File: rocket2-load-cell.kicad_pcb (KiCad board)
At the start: 2 copper layers, 69 x 67 mm, 40 parts, among them J1 SWD, J2 Screw_Terminal_01x02, U2 STM32F103C8Tx, U3 AMS1117-3.3, Y1 16MHz

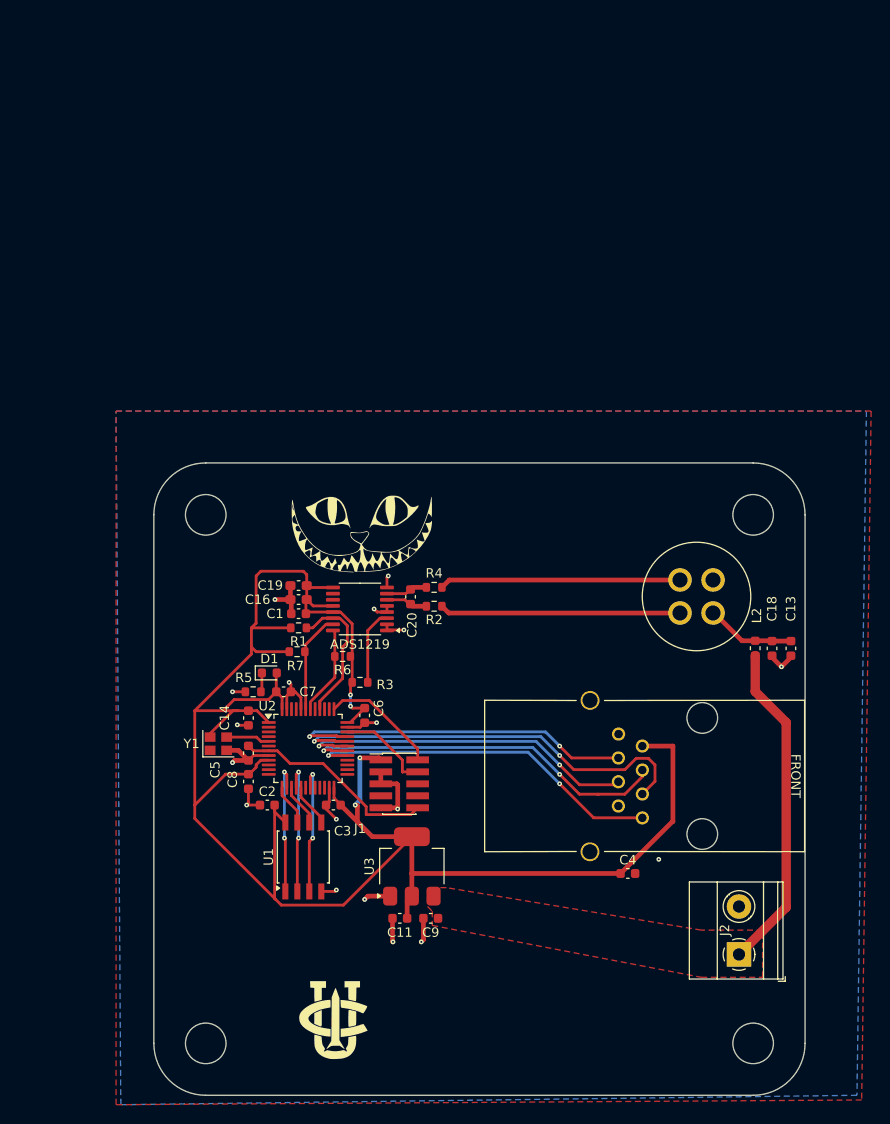
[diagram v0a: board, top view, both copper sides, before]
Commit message: PCB Updates + Schematic Adjustments
Layout, signal lines, and basis for power routing.

Added a voltage divider to the USB_VBUS pin to protect GPIO.
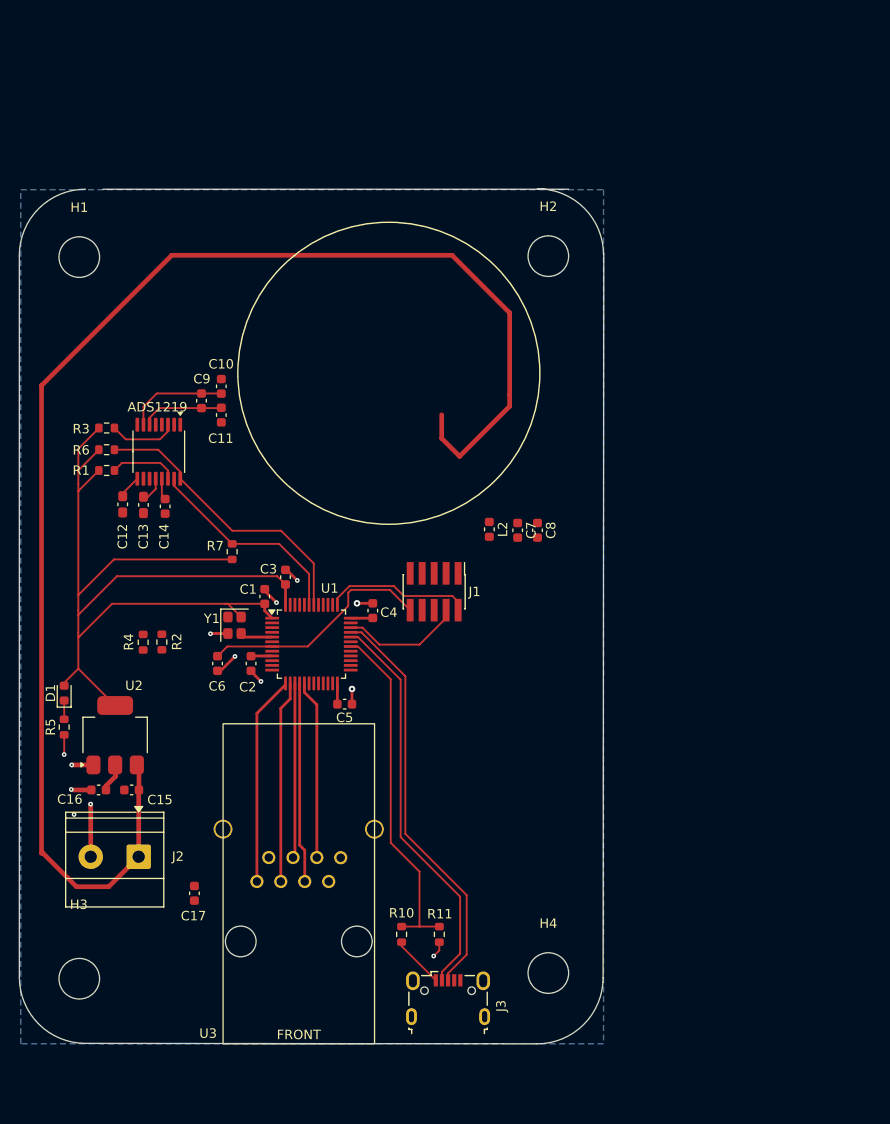
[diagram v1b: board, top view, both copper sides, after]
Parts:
- removed C18: 10uF, Capacitor_SMD:C_0603_1608Metric
- removed C19: 0.1uF, Capacitor_SMD:C_0603_1608Metric_Pad1.08x0.95mm_HandSolder
- removed C20: 0.1uF, Capacitor_SMD:C_0603_1608Metric
- removed G***: LOGO, UCILIB:uci_rocket_logo
- removed G***: LOGO, UCILIB:cat_logo
- removed GX12: ~, UCIRP-KiCAD-Lib:gx12
- removed U5: ~, GSE:GC-XPORT
- added C10: 0.1uF, Capacitor_SMD:C_0603_1608Metric, F.Cu at (127.7, 73.9)
- added C12: 0.1uF, Capacitor_SMD:C_0603_1608Metric_Pad1.08x0.95mm_HandSolder, F.Cu at (117.2, 86.4)
- added C15: 22uF, Capacitor_SMD:C_0603_1608Metric, F.Cu at (118.2, 116.7)
- added C17: 4.7uF, Capacitor_SMD:C_0603_1608Metric, F.Cu at (124.8, 127.6)
- added J3: 629105150521, Connector_USB:USB_Micro-B_Wuerth_629105150521, F.Cu at (151.7, 138.7)
- added R10: 10K, Resistor_SMD:R_0603_1608Metric, F.Cu at (146.8, 131.9)
- added R11: 10K, Resistor_SMD:R_0603_1608Metric, F.Cu at (150.8, 131.9)
- C1: value 0.1uF -> 100nF
- C11, C9: value 22uF -> 0.1uF
- C13: value 100nF -> 0.1uF; footprint Capacitor_SMD:C_0603_1608Metric -> Capacitor_SMD:C_0603_1608Metric_Pad1.08x0.95mm_HandSolder
- C14: value 100nF -> 0.1uF
- C16: value 0.1uF -> 22uF; footprint Capacitor_SMD:C_0603_1608Metric_Pad1.08x0.95mm_HandSolder -> Capacitor_SMD:C_0603_1608Metric
- C4: value 4.7uF -> 100nF
- C8: value 100nF -> 10uF
- R2, R4: value 100 -> 330
- U1: value ~ -> STM32F103C8Tx; footprint Package_SO:SOIC-8W_5.3x5.3mm_P1.27mm -> Package_QFP:LQFP-48_7x7mm_P0.5mm
- U2: value STM32F103C8Tx -> AMS1117-3.3; footprint Package_QFP:LQFP-48_7x7mm_P0.5mm -> Package_TO_SOT_SMD:SOT-223-3_TabPin2
- U3: value AMS1117-3.3 -> ~; footprint Package_TO_SOT_SMD:SOT-223-3_TabPin2 -> UCIRP-KiCAD-Lib:GC-XPORT
- moved H1 109.7 mm to (112.6, 60.2)
- moved H3 86.7 mm to (112.6, 136.7)
- moved C13 70.3 mm to (119.4, 86.5)
- moved J2 64.4 mm to (118.9, 123.7), turned to 180 degrees
- moved C9 60.0 mm to (125.5, 75.4), turned to 90 degrees
- moved C11 56.6 mm to (127.7, 76.9), turned to 90 degrees
- moved H2 45.5 mm to (162.3, 60.1)
- moved C8 40.6 mm to (161.2, 89.1), turned to -90 degrees
- moved C4 38.8 mm to (143.7, 97.7), turned to -90 degrees
- moved R3 38.0 mm to (115.5, 78.3)
- moved H4 37.1 mm to (162.3, 136.1)
- moved R6 33.2 mm to (115.5, 80.6), turned to 0 degrees
- moved R4 31.4 mm to (119.4, 101.0), turned to 90 degrees
- moved L2 30.9 mm to (156.1, 89.0)
- moved C7 30.1 mm to (159.1, 89.1), turned to -90 degrees
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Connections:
- C11 pad 2: +3.3V -> Net-(ADS1219-AIN3)
- C13 pad 1: VLC -> +3.3V
- C16 pad 1: +3.3V -> GND
- C16 pad 2: GND -> +3.3V
- C4 pad 1: +3.3V -> GND
- C4 pad 2: GND -> +3.3V
- C5 pad 2: NRST -> +3.3V
- C6 pad 2: +3.3V -> NRST
- C7 pad 1: GND -> VLC
- C7 pad 2: +3.3V -> GND
- C8 pad 1: GND -> VLC
- C8 pad 2: +3.3V -> GND
- C9 pad 1: GND -> Net-(ADS1219-AIN3)
- C9 pad 2: VBUS -> Net-(ADS1219-AIN2)
- U1 pad 1: MEM_CS -> +3.3V
- U1 pad 2: MEM_MISO -> unconnected-(U1-PC13-Pad2)
- U1 pad 3: MEM_WP -> unconnected-(U1-PC14-Pad3)
- U1 pad 4: GND -> unconnected-(U1-PC15-Pad4)
- U1 pad 5: MEM_MOSI -> HSE_IN
- U1 pad 6: MEM_SCK -> unconnected-(U1-PD1-Pad6)
- U1 pad 7: MEM_HOLD -> NRST
- U1 pad 8: +3.3V -> GND
- U2 pad 1: +3.3V -> GND
- U2 pad 2: unconnected-(U2-PC13-Pad2) -> +3.3V
- U2 pad 3: unconnected-(U2-PC14-Pad3) -> VBUS
- U3 pad 3: VBUS -> ETH_~{RST}
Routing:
- net VBUS: track 35.1 -> 152.9 mm
- net +3.3V: track 214.6 -> 127.8 mm, vias 4 -> 0
- net USB_D+: track 0.00 -> 43.9 mm
- net USB_D-: track 0.00 -> 42.6 mm
- net Net-(U1-PA9): track 0.00 -> 37.1 mm
- net GND: track 55.9 -> 26.5 mm, vias 18 -> 13
- net AIN+: track 25.6 -> 0.00 mm
- net AIN-: track 25.5 -> 0.00 mm
- net ETH_RTS: track 45.8 -> 21.4 mm, vias 2 -> 0
- net ETH_TX: track 40.0 -> 18.5 mm, vias 2 -> 0
- net ADS_CLK: track 9.49 -> 30.9 mm
- net ETH_~{RST}: track 38.2 -> 19.0 mm, vias 2 -> 0
- net ETH_CTS: track 38.3 -> 22.2 mm, vias 2 -> 0
- net ETH_RX: track 36.6 -> 21.2 mm, vias 2 -> 0
- net MEM_MISO: track 14.5 -> 0.00 mm, vias 2 -> 0
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- removed copper zone on F.Cu, net GND
- removed copper zone on F.Cu, net VBUS
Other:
- board size 69 x 67 mm -> 61.9 x 90.6 mm

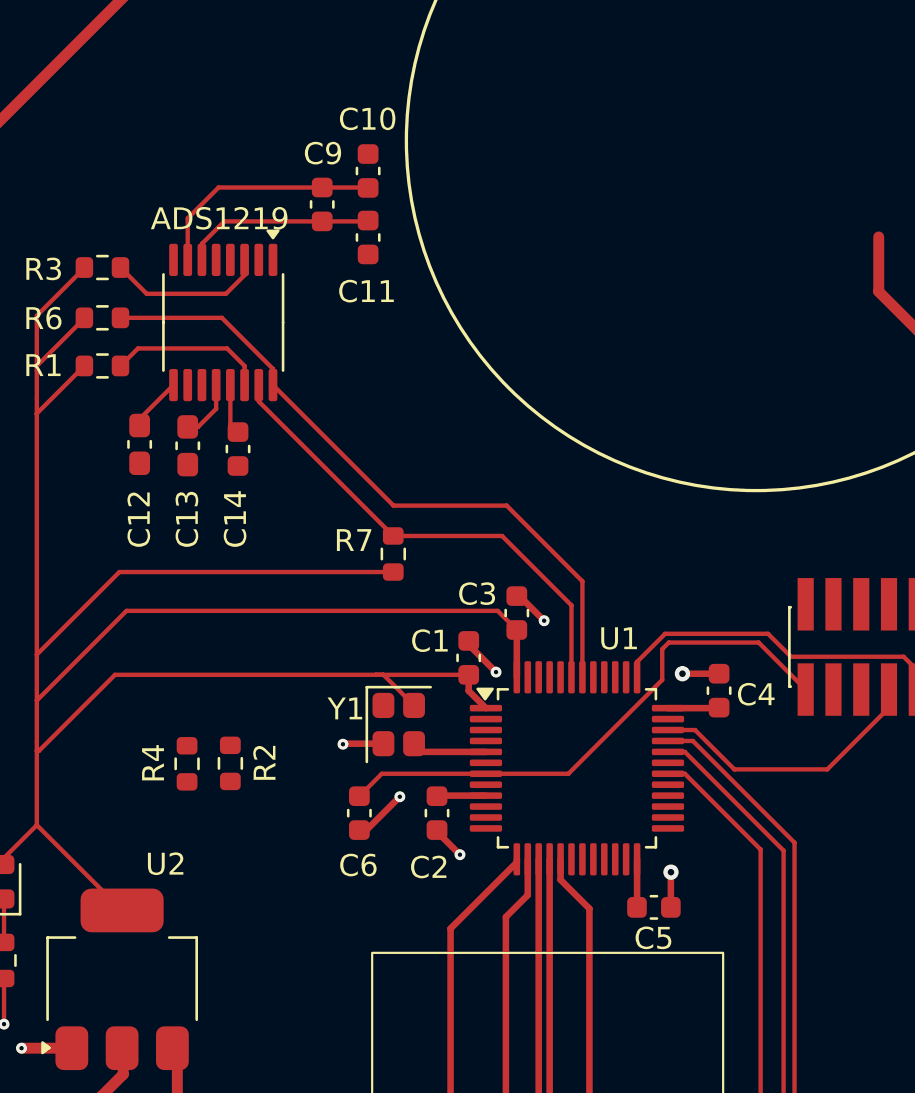
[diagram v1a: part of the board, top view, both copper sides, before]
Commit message: Adjustments to Decaps
More direct GND access
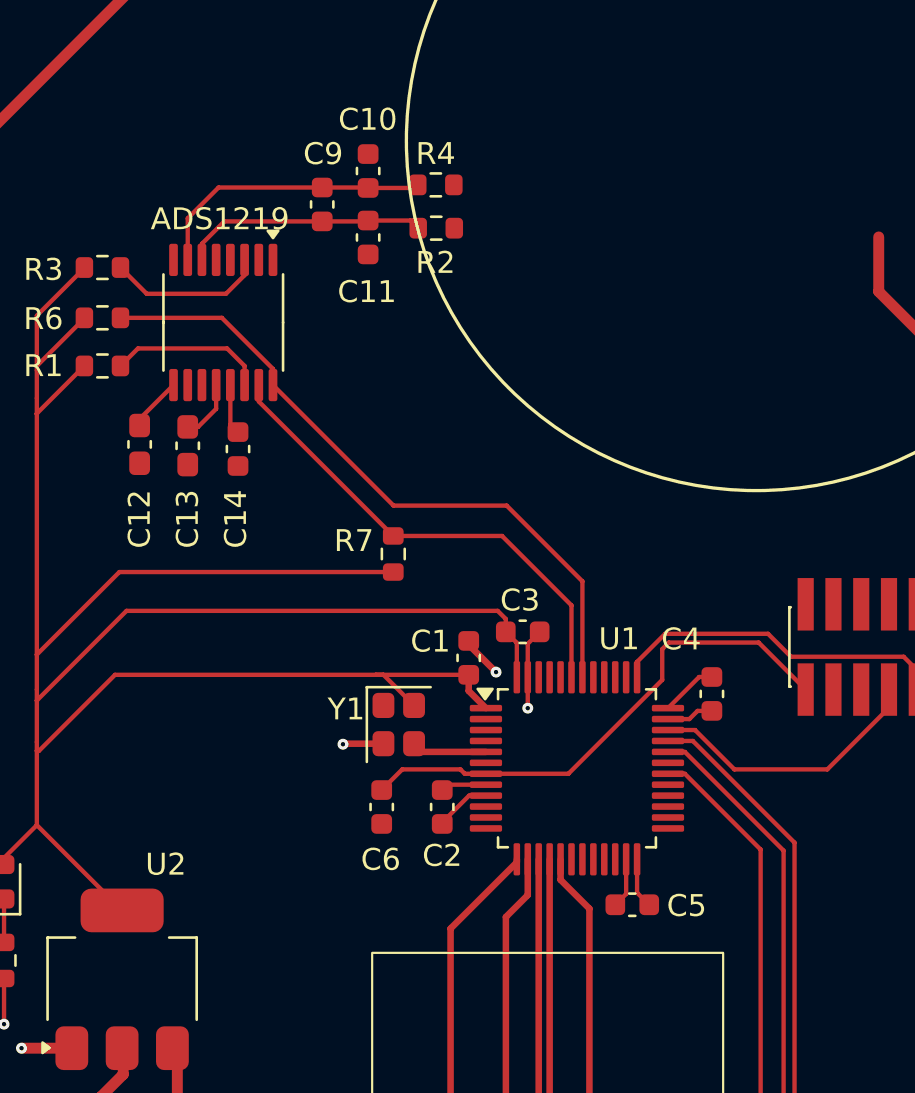
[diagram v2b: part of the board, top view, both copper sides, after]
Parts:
- moved R4 28.8 mm to (130.7, 74.5), turned to 180 degrees
- moved R2 26.2 mm to (130.8, 76.5), turned to 180 degrees
- moved C6 1.06 mm to (128.3, 103.0)
- moved C5 1.00 mm to (139.7, 107.4), turned to 0 degrees
- moved C3 0.90 mm to (134.7, 95.0), turned to 180 degrees
- moved C2 0.37 mm to (131.0, 103.0), turned to -90 degrees
- moved C4 0.36 mm to (143.4, 97.8), turned to 90 degrees
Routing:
- net Net-(ADS1219-AIN3): track 8.86 -> 11.3 mm
- net Net-(ADS1219-AIN2): track 10.7 -> 13.1 mm
- net GND: track 26.5 -> 28.0 mm, vias 13 -> 9
- net NRST: track 25.0 -> 24.1 mm

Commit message: Power Routing Updates
W.I.P.
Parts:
- moved R5 13.4 mm to (123.8, 114.1)
- moved D1 13.4 mm to (123.8, 110.5)
- moved H3 4.40 mm to (117.0, 136.5)
- moved H1 4.40 mm to (117.0, 60.2)
- moved J2 2.11 mm to (121.0, 123.8)
- moved C15 2.07 mm to (120.2, 116.9)
- moved C16 2.07 mm to (116.7, 116.9)
- moved U2 2.07 mm to (118.5, 111.1)
- moved C17 1.97 mm to (125.8, 129.3), turned to -90 degrees
- moved H4 0.45 mm to (162.3, 136.5)
- moved C14 0.20 mm to (121.5, 86.6)
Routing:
- net ADS_DRDY: track 7.21 -> 29.8 mm, vias 0 -> 1
- net +3.3V: track 128.2 -> 150.3 mm
- net GND: track 28.0 -> 36.5 mm, vias 9 -> 16
- net VBUS: track 152.9 -> 147.4 mm
- net Net-(D1-K): track 1.99 -> 0.00 mm
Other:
- board size 61.9 x 90.6 mm -> 58.2 x 90.6 mm

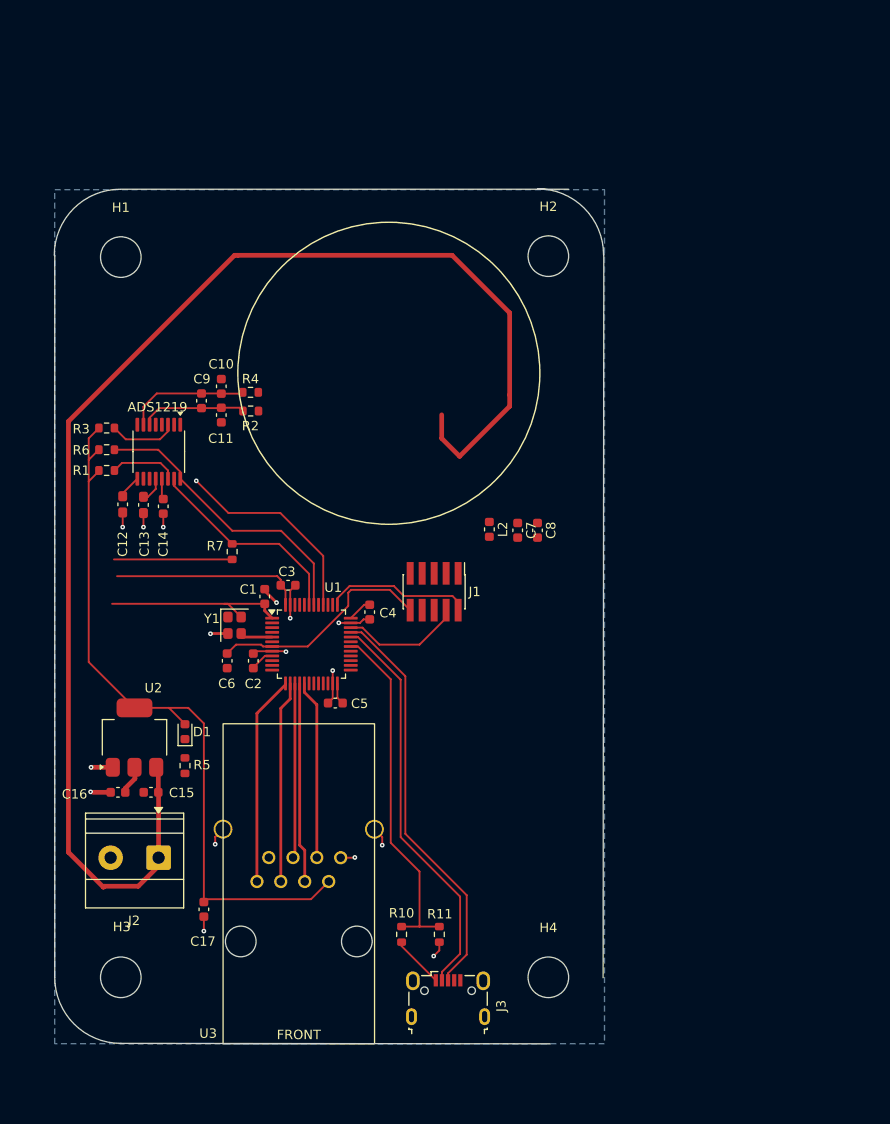
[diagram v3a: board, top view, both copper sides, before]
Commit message: W.I.P. PCB adjustments
Reducing e-footprint and signal line length to ADC - also corrected some previous issues with signal + power routing
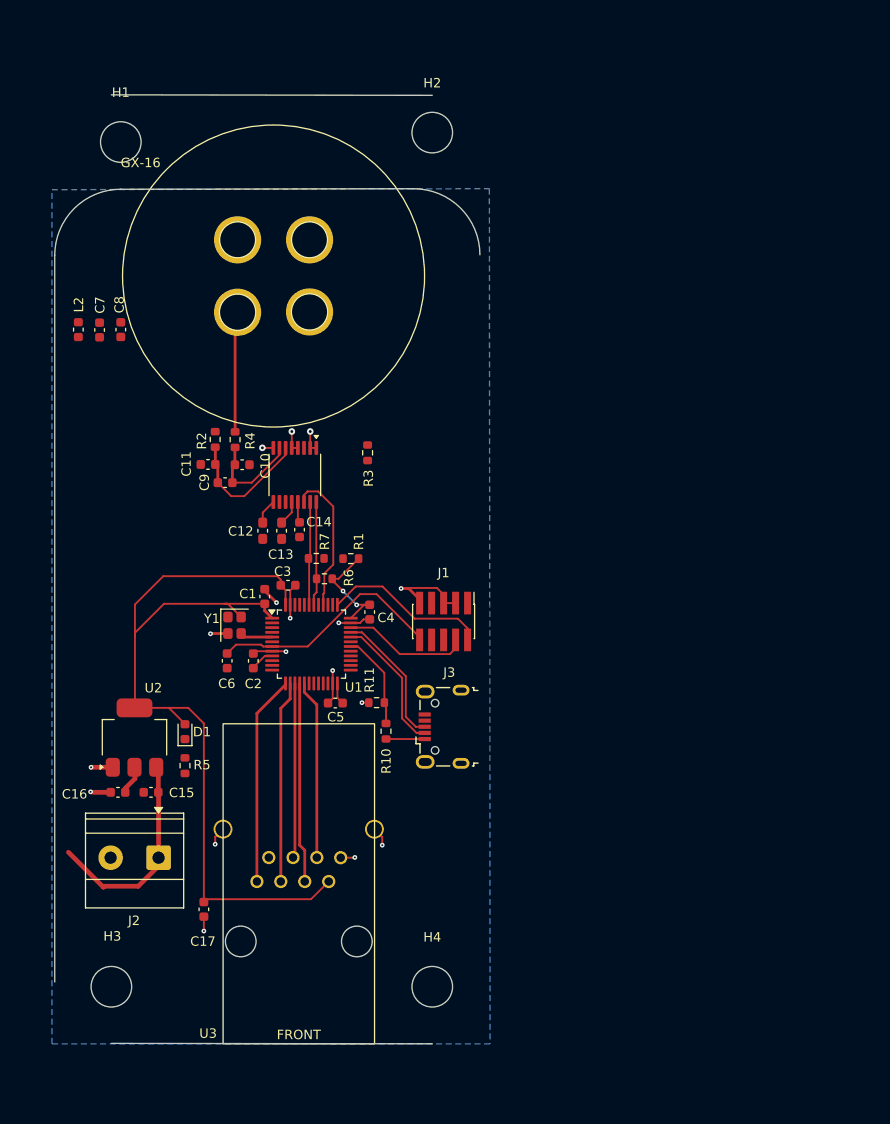
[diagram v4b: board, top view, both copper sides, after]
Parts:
- added GX-16: ~, UCIRP-KiCAD-Lib:GX16-4, F.Cu at (133.2, 62.2)
- moved C7 49.1 mm to (114.8, 67.9)
- moved C8 49.0 mm to (117.0, 67.9)
- moved L2 48.4 mm to (112.5, 67.9)
- moved J3 28.8 mm to (151.1, 110.0), turned to 90 degrees
- moved R3 27.8 mm to (143.2, 80.9), turned to -90 degrees
- moved R1 27.5 mm to (141.4, 92.1), turned to 0 degrees
- moved R6 26.8 mm to (138.6, 94.3), turned to 180 degrees
- moved R11 25.4 mm to (144.1, 107.4), turned to 0 degrees
- moved R10 21.6 mm to (145.1, 110.4)
- moved H2 18.0 mm to (150.0, 47.0)
- moved C12 15.1 mm to (132.0, 89.2)
- moved C13 14.9 mm to (134.0, 89.2)
- moved C14 14.6 mm to (135.9, 89.1)
- moved ADS1219 14.6 mm to (135.4, 83.3)
- moved H4 12.3 mm to (150.0, 137.5)
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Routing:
- net VBUS: track 147.4 -> 22.6 mm
- net USB_D+: track 43.9 -> 14.5 mm
- net +3.3V: track 150.3 -> 120.9 mm, vias 0 -> 2
- net USB_D-: track 42.6 -> 14.6 mm
- net Net-(U1-PA9): track 37.1 -> 10.4 mm
- net ADS_CLK: track 30.9 -> 11.0 mm
- net ADS_DRDY: track 29.8 -> 15.5 mm, vias 1 -> 0
- net AIN+: track 0.00 -> 12.8 mm
- net ADS_DATA: track 22.2 -> 11.0 mm
- net GND: track 36.5 -> 47.0 mm, vias 16 -> 17
- net Net-(ADS1219-RESET): track 7.14 -> 0.00 mm
- net Net-(ADS1219-AIN3): track 11.3 -> 14.2 mm
- net Net-(ADS1219-AIN2): track 13.1 -> 10.8 mm
- net DEBUG_SWDIO: track 15.6 -> 17.9 mm
- net USB_VBUS: track 5.87 -> 4.10 mm
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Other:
- board size 58.2 x 90.6 mm -> 45.1 x 100.6 mm
